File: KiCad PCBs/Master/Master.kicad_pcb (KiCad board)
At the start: 2 copper layers, 81.9 x 55.2 mm, 24 parts

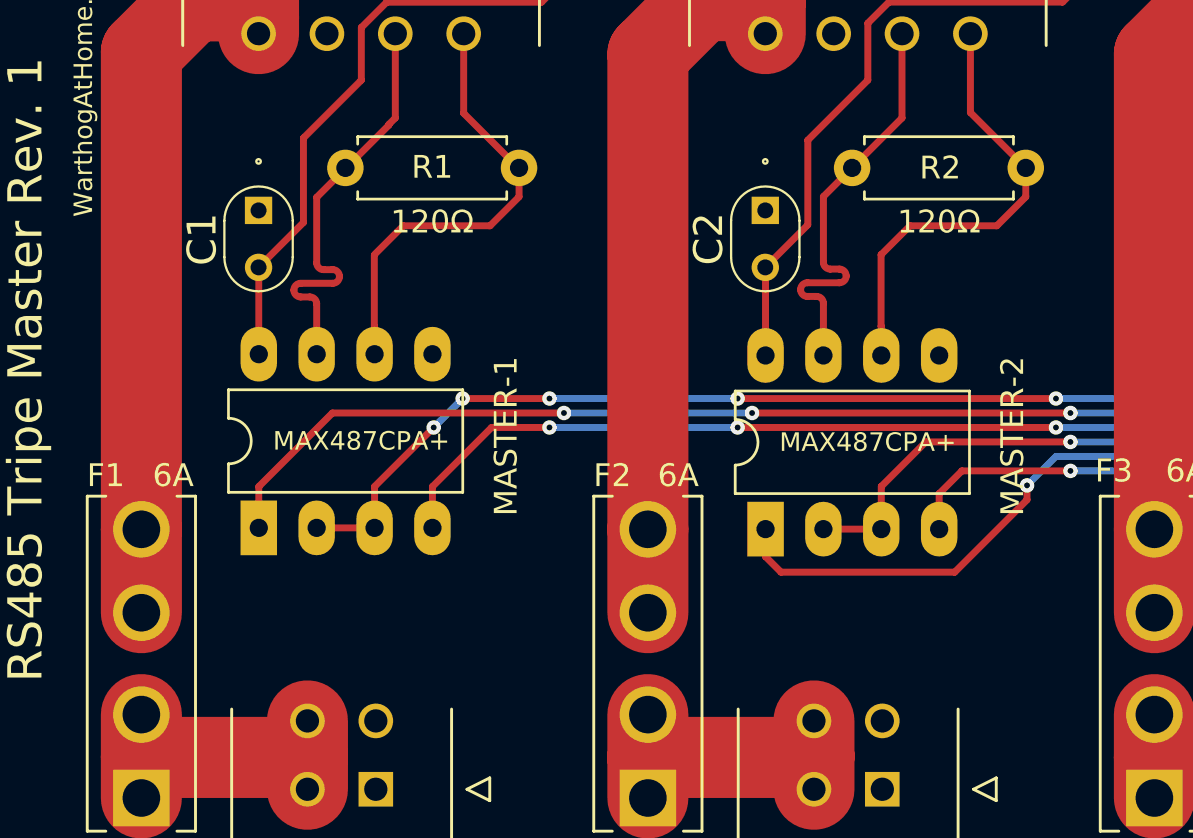
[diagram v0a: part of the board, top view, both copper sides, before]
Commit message: Added power status LEDs to Master PCB
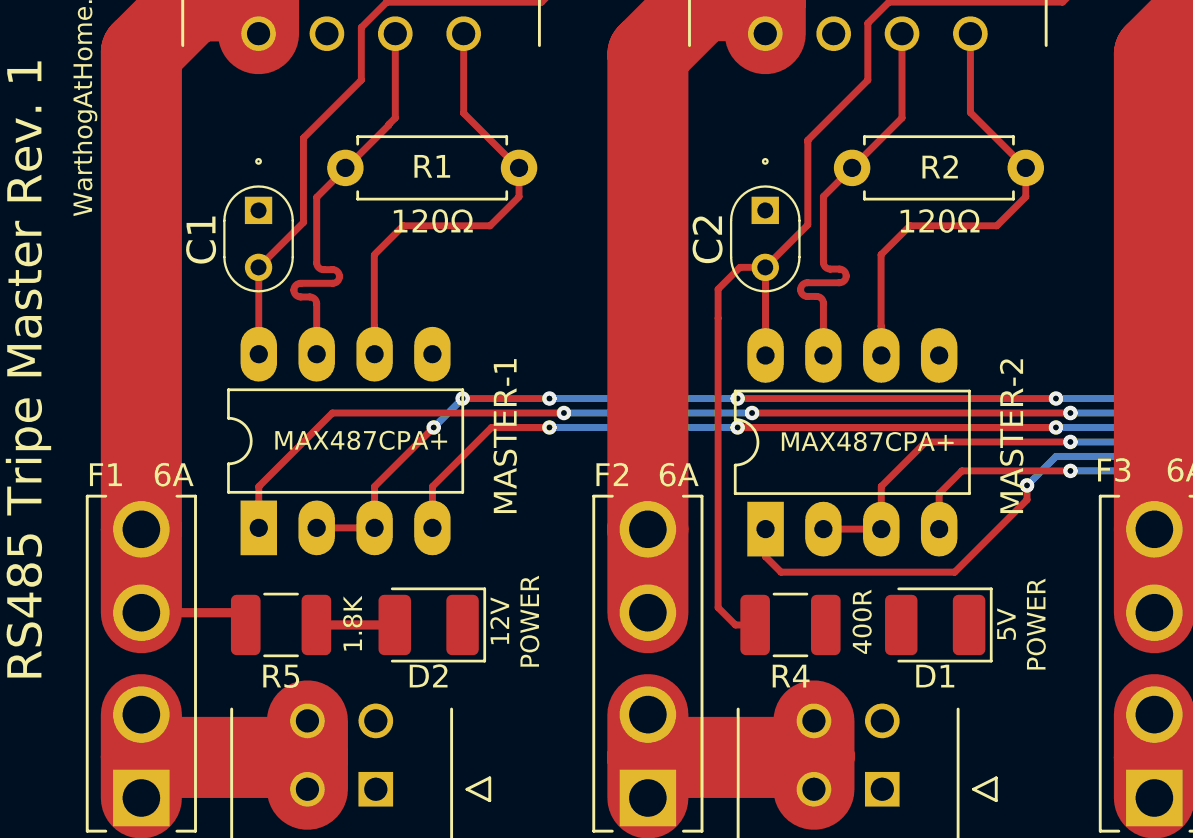
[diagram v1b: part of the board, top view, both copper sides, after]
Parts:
- added D1: GREEN, LED_SMD:LED_1210_3225Metric_Pad1.42x2.65mm_HandSolder, F.Cu at (148.6, 111.3)
- added D2: GREEN, LED_SMD:LED_1210_3225Metric_Pad1.42x2.65mm_HandSolder, F.Cu at (126.4, 111.3)
- added R4: 400R, Resistor_SMD:R_1210_3225Metric_Pad1.30x2.65mm_HandSolder, F.Cu at (142.2, 111.3)
- added R5: 1.8K, Resistor_SMD:R_1210_3225Metric_Pad1.30x2.65mm_HandSolder, F.Cu at (119.9, 111.3)
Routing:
- net +5V: track 155.4 -> 173.7 mm
- net 12V_Fused: track 113.0 -> 117.8 mm
- net Net-(D2-Pad2): track 0.00 -> 3.44 mm
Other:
- board text added: "12V POWER"
- board text added: "5V POWER"

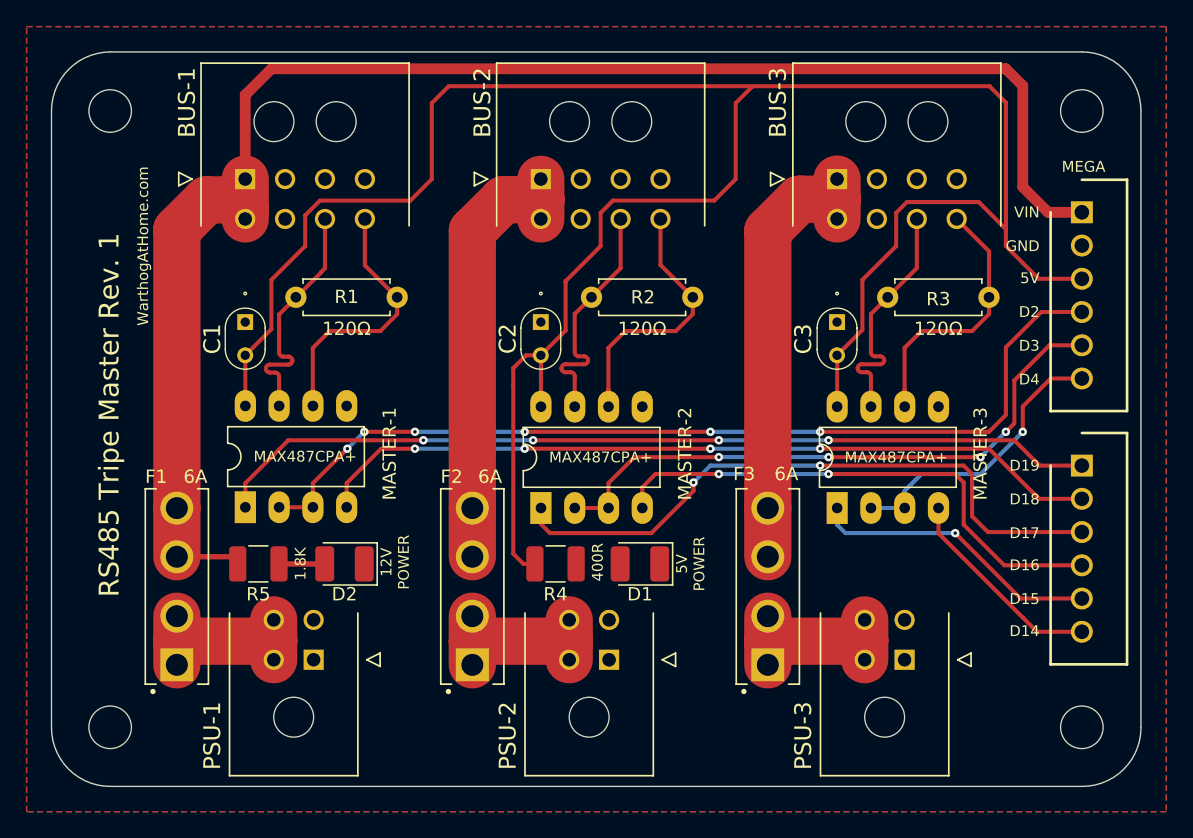
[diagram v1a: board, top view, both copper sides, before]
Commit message: Added power status LED to each bus
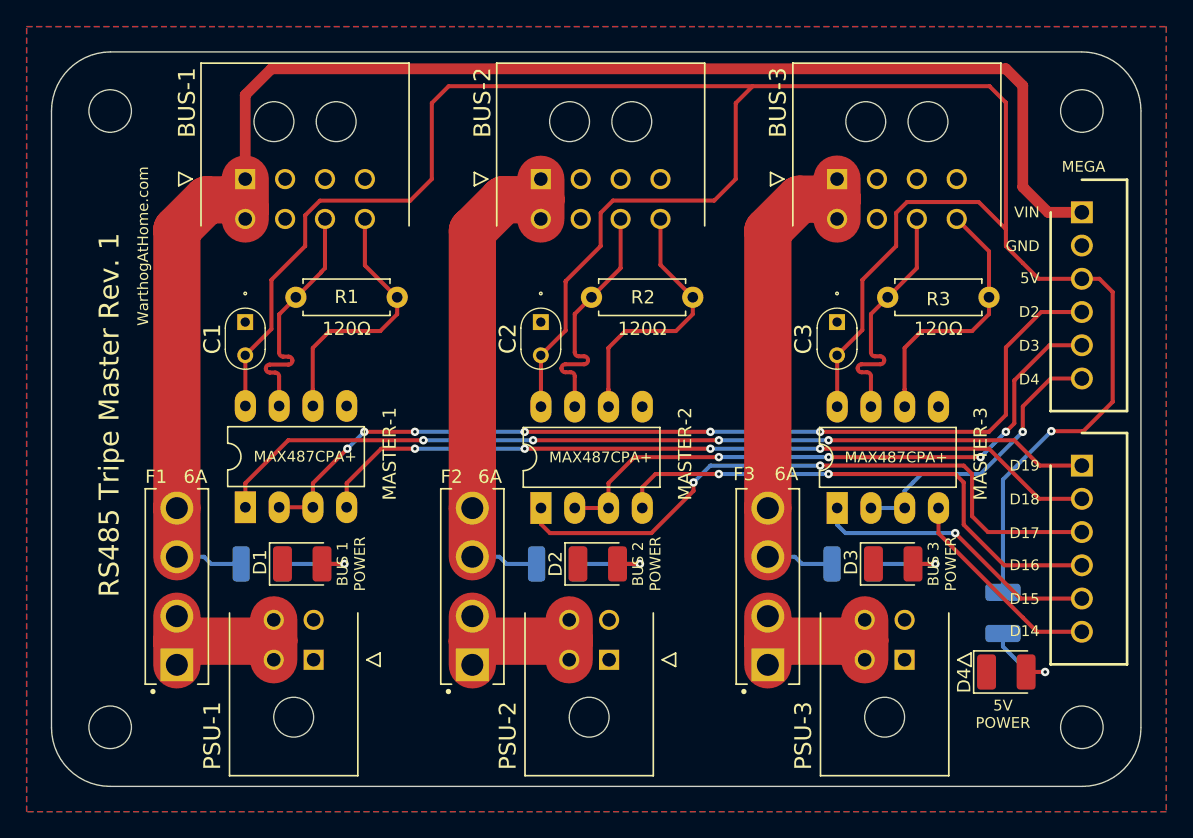
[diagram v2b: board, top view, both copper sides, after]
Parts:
- added D3: GREEN, LED_SMD:LED_1210_3225Metric_Pad1.42x2.65mm_HandSolder, F.Cu at (167.6, 111.3)
- added D4: GREEN, LED_SMD:LED_1210_3225Metric_Pad1.42x2.65mm_HandSolder, F.Cu at (176.1, 119.4)
- added R6: 1.8K, Resistor_SMD:R_1210_3225Metric_Pad1.30x2.65mm_HandSolder, B.Cu at (164.6, 111.3)
- added R7: 400R, Resistor_SMD:R_1210_3225Metric_Pad1.30x2.65mm_HandSolder, B.Cu at (175.9, 114.9)
- R4: value 400R -> 1.8K; moved to B.Cu
- R5: moved to B.Cu
- moved D1 25.4 mm to (123.2, 111.3), turned to 0 degrees
- moved R5 22.5 mm to (142.4, 111.3)
- moved R4 22.1 mm to (120.1, 111.3)
- moved D2 19.0 mm to (145.4, 111.3), turned to 0 degrees
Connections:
- D1 pad 1: GND -> unconnected-(D1-Pad1)
- D2 pad 1: GND -> unconnected-(D2-Pad1)
- R4 pad 2: +5V -> 12V_Fused
- R5 pad 2: 12V_Fused -> /12V_2_Fused
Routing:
- net +5V: track 173.7 -> 185.5 mm, vias 0 -> 1
- net Net-(D1-Pad2): track 0.00 -> 6.49 mm, vias 0 -> 1
- net Net-(D4-Pad2): track 0.00 -> 6.39 mm, vias 0 -> 1
- net Net-(D3-Pad2): track 0.00 -> 6.36 mm, vias 0 -> 1
- net /12V_2_Fused: track 33.7 -> 38.7 mm
- net /12V_3_Fused: track 33.7 -> 38.8 mm
- net Net-(D2-Pad2): track 3.44 -> 6.36 mm, vias 0 -> 1
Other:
- board text added: "BUS 1 POWER"
- board text added: "BUS 2 POWER"
- board text added: "BUS 3 POWER"
- board text removed: "12V POWER"

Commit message: Master PCB Adjustments
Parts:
- moved BUS-1 1.06 mm to (118.9, 81.2)
- moved BUS-2 1.06 mm to (141.1, 81.2)
- moved BUS-3 1.06 mm to (163.4, 81.2)
- moved F2 0.95 mm to (136.0, 113.9)
- moved F3 0.95 mm to (158.2, 113.9)
- moved PSU-2 0.95 mm to (146.3, 119.4)
- moved PSU-3 0.95 mm to (168.5, 119.4)
- moved F1 0.92 mm to (113.8, 113.9)
- moved PSU-1 0.92 mm to (124.0, 119.4)
- moved HOLE-1 0.79 mm to (108.0, 77.2)
- moved HOLE-3 0.79 mm to (108.0, 123.5)
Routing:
- net 12V_Fused: track 117.9 -> 82.9 mm
- net /12V_3_Fused: track 38.8 -> 5.06 mm
- net /12V_2_Fused: track 38.7 -> 5.06 mm
- net +12V_3: track 14.0 -> 0.00 mm
- net +12V_2: track 14.0 -> 0.00 mm
- net +12V: track 13.9 -> 0.00 mm
- net +5V: track 185.5 -> 192.1 mm
- net RS485-3-B: track 18.7 -> 20.1 mm
- net RS485-2-A: track 20.0 -> 21.1 mm
- net RS485-1-B: track 18.6 -> 19.7 mm
- net RS485-3-A: track 20.0 -> 21.1 mm
- net RS485-2-B: track 18.7 -> 19.8 mm
- net RS485-1-A: track 19.9 -> 21.0 mm
- net MEGA_D2: track 70.5 -> 71.0 mm
- added copper zone on F.Cu, net +12V
- added copper zone on F.Cu, net +12V_2
- added copper zone on F.Cu, net +12V_3
- added copper zone on F.Cu, net /12V_2_Fused
- added copper zone on F.Cu, net /12V_3_Fused
- added copper zone on F.Cu, net 12V_Fused
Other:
- board size 81.9 x 55.2 mm -> 82.8 x 55.2 mm

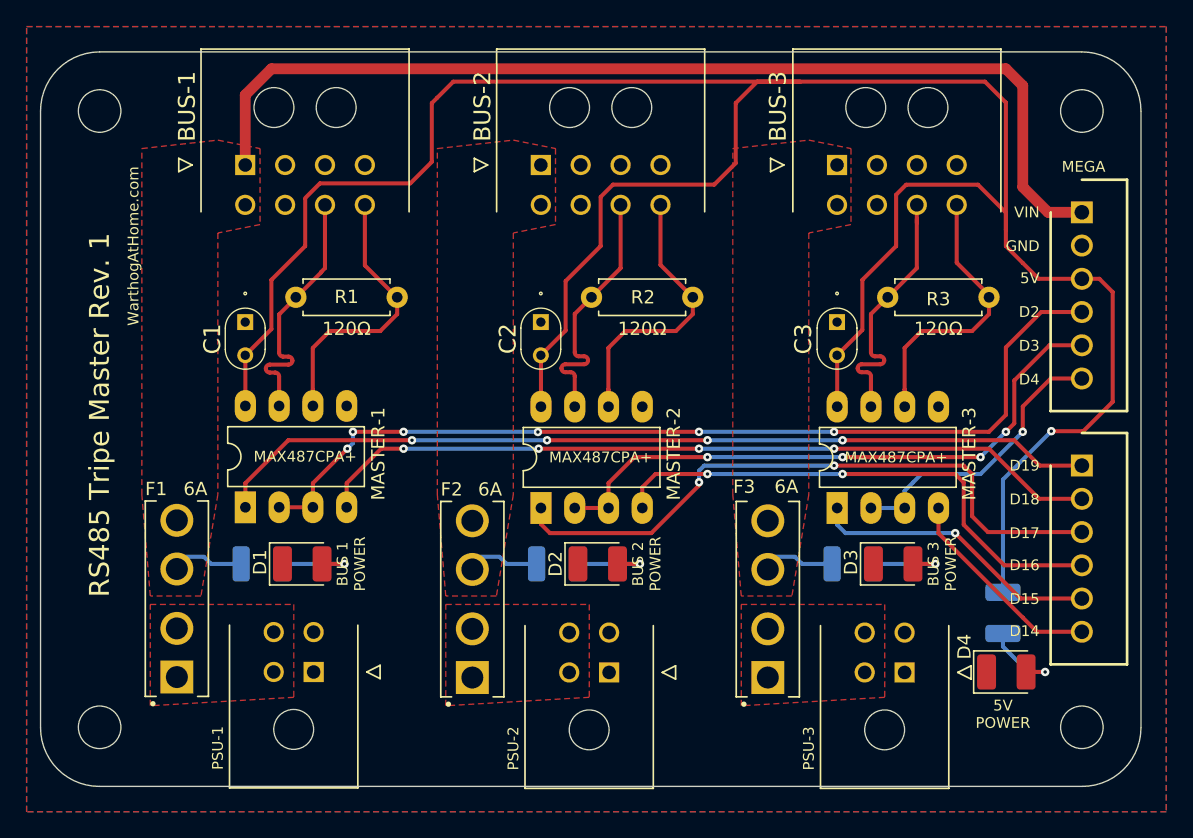
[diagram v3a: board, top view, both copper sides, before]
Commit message: Updated Master PCB and completed first version of Hub
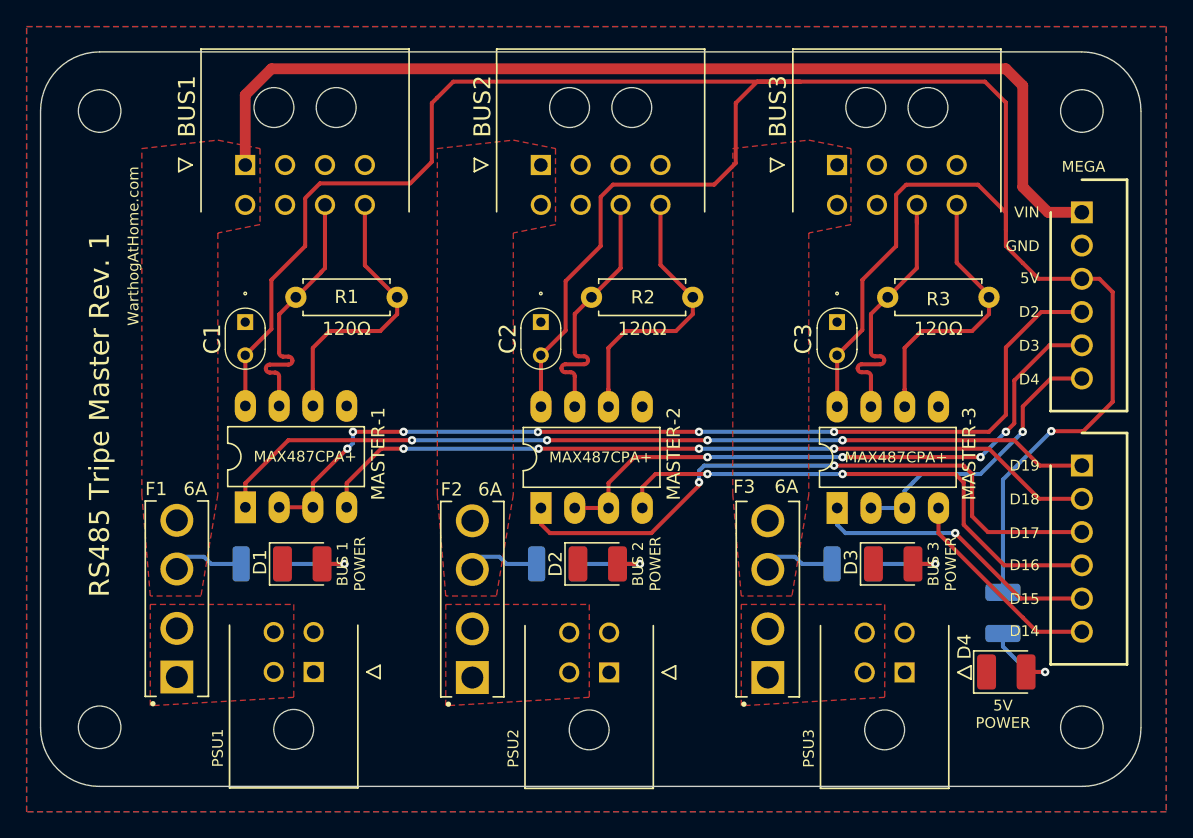
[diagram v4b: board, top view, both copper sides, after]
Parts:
- renumbered BUS-1 to BUS1, BUS-2 to BUS2, BUS-3 to BUS3, PSU-1 to PSU1, PSU-2 to PSU2, PSU-3 to PSU3
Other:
- rule pad_to_mask_clearance: 0.0508 -> 0
